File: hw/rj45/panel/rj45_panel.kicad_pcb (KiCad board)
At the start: 6 copper layers, 71.4 x 107 mm, 471 parts, among them J1 SFP edge (INF-8074i), J2 KH-RJ45-58-8P8C, T1 LP72450ANL, U1 RTL8221B-VB-CG, U2 STM32G031F6P6, U3 TPS62822DLC, U4 TPS22918DBVR, X1 MST8011AI-72-33E25

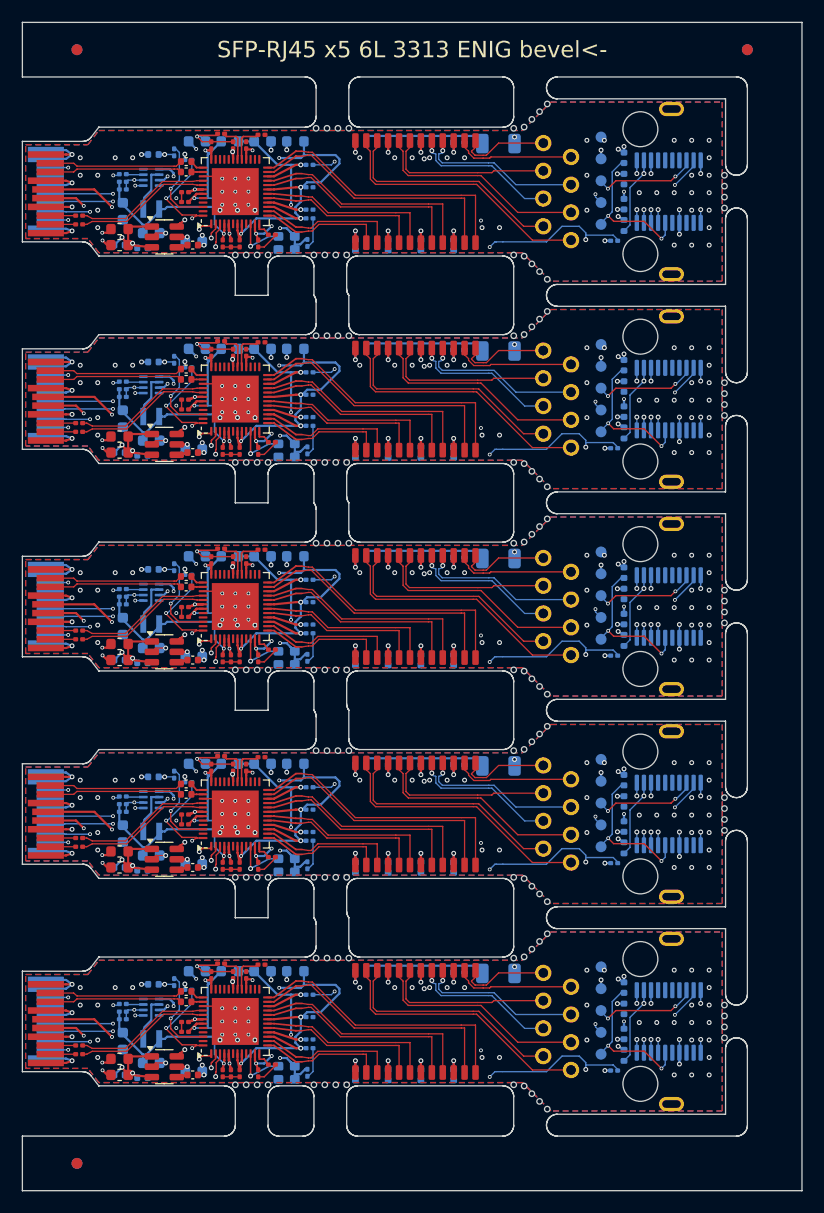
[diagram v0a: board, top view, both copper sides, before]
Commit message: RJ45: PHY address straps on LED0/1/2, re-routed: DRC 0 / 0, KiCad 9 PASS, panel 0 errors
The RTL8221B's CONFIG pins have no internal pulls (datasheet 7.18), so
LED0/1/2 (PHYAD[2:0]) floated. R19-R21, 4.7k to ground: PHYAD 000, which the
PHY maps to address 1 (Table 16 note 2), the firmware's address. Three 0201s
above pins 33-35; C16 moved underneath its via, C17 0.3 mm west.

R11 (INT's pull-up) moved under INT's In2 via. Two links the router left
open are laid by hand before routing (VCCR finger to FB2 through In2, R4's
feedback end through In2); one fresh Freerouting session around them is
kept as rj45.ses.

sfpgen, for board rebuilds:
- plane_dogbones' no-room fallback no longer lays a pad-centre copy of a
  link the pad already has through hand-laid copper (it ran a +3V3 stub
  into the edge strip, and the n <= n0 DRC count let it through);
- drop_duplicate_plane_vias also drops GND router vias inside a locked GND
  via, and the later of two locked same-net vias on top of each other.

KiCad 7 DRC 0 / 0 unconnected, ERC 0; KiCad 9 DRC 0 errors, parity clean,
ERC 0 errors; panel 0 errors, 0 unconnected; edge pins as SFF-8419.
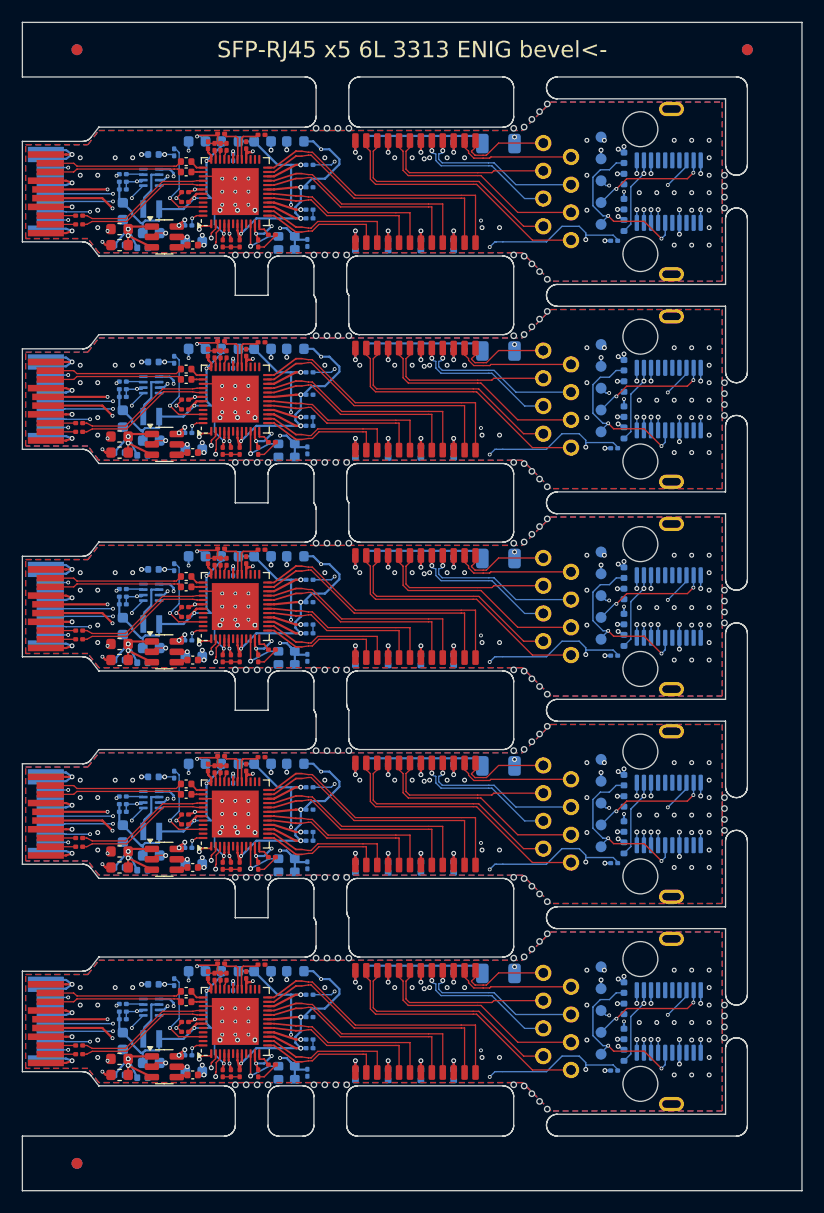
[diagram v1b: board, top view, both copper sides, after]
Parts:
- removed the C16 at (132.1, 88.2)
- removed the C16 at (132.1, 50.2)
- removed the C16 at (132.1, 107.2)
- removed the C16 at (132.1, 69.2)
- removed the C16 at (132.1, 31.2)
- removed the C17 at (130.1, 88.2)
- removed the C17 at (130.1, 69.2)
- removed the C17 at (130.1, 50.2)
- removed the C17 at (130.1, 107.2)
- removed the C17 at (130.1, 31.2)
- removed KiKit_MB_15_5, KiKit_MB_21_5, KiKit_MB_27_5, KiKit_MB_3_5, KiKit_MB_9_5: NPTH, NPTH
- removed the R11 at (128.0, 32.6)
- removed the R11 at (128.0, 51.6)
- removed the R11 at (128.0, 108.6)
- removed the R11 at (128.0, 89.6)
- removed the R11 at (128.0, 70.6)
- added C16: 100nF, Capacitor_SMD:C_0201_0603Metric, B.Cu at (132.1, 32.4)
- added C16: 100nF, Capacitor_SMD:C_0201_0603Metric, B.Cu at (132.1, 108.3)
- added C16: 100nF, Capacitor_SMD:C_0201_0603Metric, B.Cu at (132.1, 51.4)
- added C16: 100nF, Capacitor_SMD:C_0201_0603Metric, B.Cu at (132.1, 89.3)
- added C16: 100nF, Capacitor_SMD:C_0201_0603Metric, B.Cu at (132.1, 70.3)
- added C17: 100nF, Capacitor_SMD:C_0201_0603Metric, F.Cu at (129.8, 50.2)
- added C17: 100nF, Capacitor_SMD:C_0201_0603Metric, F.Cu at (129.8, 69.2)
- added C17: 100nF, Capacitor_SMD:C_0201_0603Metric, F.Cu at (129.8, 31.2)
- added C17: 100nF, Capacitor_SMD:C_0201_0603Metric, F.Cu at (129.8, 107.2)
- added C17: 100nF, Capacitor_SMD:C_0201_0603Metric, F.Cu at (129.8, 88.2)
- added KiKit_MB_12_5: NPTH, NPTH, F.Cu at (160.9, 46.5)
- added KiKit_MB_18_5: NPTH, NPTH, F.Cu at (160.9, 65.5)
- added KiKit_MB_24_5: NPTH, NPTH, F.Cu at (160.9, 84.5)
- added KiKit_MB_30_5: NPTH, NPTH, F.Cu at (160.9, 103.5)
- added KiKit_MB_6_5: NPTH, NPTH, F.Cu at (160.9, 27.5)
- added R11: 4.7k, Resistor_SMD:R_0201_0603Metric, B.Cu at (128.0, 38.6)
- added R11: 4.7k, Resistor_SMD:R_0201_0603Metric, B.Cu at (128.0, 76.6)
- added R11: 4.7k, Resistor_SMD:R_0201_0603Metric, B.Cu at (128.0, 95.6)
- added R11: 4.7k, Resistor_SMD:R_0201_0603Metric, B.Cu at (128.0, 57.6)
- added R11: 4.7k, Resistor_SMD:R_0201_0603Metric, B.Cu at (128.0, 114.6)
- added R19: 4.7k, Resistor_SMD:R_0201_0603Metric, F.Cu at (131.5, 50.4)
- added R19: 4.7k, Resistor_SMD:R_0201_0603Metric, F.Cu at (131.5, 107.4)
- added R19: 4.7k, Resistor_SMD:R_0201_0603Metric, F.Cu at (131.5, 88.4)
- added R19: 4.7k, Resistor_SMD:R_0201_0603Metric, F.Cu at (131.5, 69.4)
- added R19: 4.7k, Resistor_SMD:R_0201_0603Metric, F.Cu at (131.5, 31.4)
- added R20: 4.7k, Resistor_SMD:R_0201_0603Metric, F.Cu at (130.9, 50.4)
- added R20: 4.7k, Resistor_SMD:R_0201_0603Metric, F.Cu at (130.9, 107.4)
- added R20: 4.7k, Resistor_SMD:R_0201_0603Metric, F.Cu at (130.9, 88.4)
- added R20: 4.7k, Resistor_SMD:R_0201_0603Metric, F.Cu at (130.9, 69.4)
- added R20: 4.7k, Resistor_SMD:R_0201_0603Metric, F.Cu at (130.9, 31.4)
- added R21: 4.7k, Resistor_SMD:R_0201_0603Metric, F.Cu at (130.4, 107.4)
- added R21: 4.7k, Resistor_SMD:R_0201_0603Metric, F.Cu at (130.4, 88.4)
- added R21: 4.7k, Resistor_SMD:R_0201_0603Metric, F.Cu at (130.4, 50.4)
- added R21: 4.7k, Resistor_SMD:R_0201_0603Metric, F.Cu at (130.4, 69.4)
- added R21: 4.7k, Resistor_SMD:R_0201_0603Metric, F.Cu at (130.4, 31.4)
- moved KiKit_MB_13_4 37.8 mm to (139.5, 79.3)
- moved KiKit_MB_19_4 37.8 mm to (139.5, 98.3)
- moved KiKit_MB_1_4 37.8 mm to (139.5, 41.3)
- moved KiKit_MB_25_4 37.8 mm to (139.5, 117.3)
- moved KiKit_MB_7_4 37.8 mm to (139.5, 60.3)
- moved KiKit_MB_13_3 37.0 mm to (140.5, 79.3)
- moved KiKit_MB_19_3 37.0 mm to (140.5, 98.3)
- moved KiKit_MB_1_3 37.0 mm to (140.5, 41.3)
- moved KiKit_MB_25_3 37.0 mm to (140.5, 117.3)
- moved KiKit_MB_7_3 37.0 mm to (140.5, 60.3)
- moved KiKit_MB_13_2 36.2 mm to (141.5, 79.3)
- moved KiKit_MB_19_2 36.2 mm to (141.5, 98.3)
- moved KiKit_MB_1_2 36.2 mm to (141.5, 41.3)
- moved KiKit_MB_25_2 36.2 mm to (141.5, 117.3)
- moved KiKit_MB_7_2 36.2 mm to (141.5, 60.3)
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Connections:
- U1 pad 33: Board_3-unconnected-(U1-LED0/PHYAD0-Pad33) -> Board_3-LED0
- U1 pad 34: Board_3-unconnected-(U1-LED1/PHYAD1-Pad34) -> Board_3-LED1
- U1 pad 35: Board_3-unconnected-(U1-LED2/PHYAD2-Pad35) -> Board_3-LED2
- U1 pad 33: Board_4-unconnected-(U1-LED0/PHYAD0-Pad33) -> Board_4-LED0
- U1 pad 34: Board_4-unconnected-(U1-LED1/PHYAD1-Pad34) -> Board_4-LED1
- U1 pad 35: Board_4-unconnected-(U1-LED2/PHYAD2-Pad35) -> Board_4-LED2
- U1 pad 33: Board_0-unconnected-(U1-LED0/PHYAD0-Pad33) -> Board_0-LED0
- U1 pad 34: Board_0-unconnected-(U1-LED1/PHYAD1-Pad34) -> Board_0-LED1
- U1 pad 35: Board_0-unconnected-(U1-LED2/PHYAD2-Pad35) -> Board_0-LED2
- U1 pad 33: Board_2-unconnected-(U1-LED0/PHYAD0-Pad33) -> Board_2-LED0
- U1 pad 34: Board_2-unconnected-(U1-LED1/PHYAD1-Pad34) -> Board_2-LED1
- U1 pad 35: Board_2-unconnected-(U1-LED2/PHYAD2-Pad35) -> Board_2-LED2
- U1 pad 33: Board_1-unconnected-(U1-LED0/PHYAD0-Pad33) -> Board_1-LED0
- U1 pad 34: Board_1-unconnected-(U1-LED1/PHYAD1-Pad34) -> Board_1-LED1
- U1 pad 35: Board_1-unconnected-(U1-LED2/PHYAD2-Pad35) -> Board_1-LED2
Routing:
- net Board_4-PHY_INT_N: track 53.5 -> 46.1 mm, vias 3 -> 2
- net Board_3-PHY_INT_N: track 53.5 -> 46.1 mm, vias 3 -> 2
- net Board_2-PHY_INT_N: track 53.5 -> 46.1 mm, vias 3 -> 2
- net Board_0-PHY_INT_N: track 53.5 -> 46.1 mm, vias 3 -> 2
- net Board_1-PHY_INT_N: track 53.5 -> 46.1 mm, vias 3 -> 2
- net Board_3-+3V3: track 43.7 -> 40.1 mm
- net Board_4-+3V3: track 43.7 -> 40.1 mm
- net Board_2-+3V3: track 43.7 -> 40.1 mm
- net Board_0-+3V3: track 43.7 -> 40.1 mm
- net Board_1-+3V3: track 43.7 -> 40.1 mm
- net Board_3-GND: track 45.3 -> 42.8 mm
- net Board_4-GND: track 45.3 -> 42.8 mm
- net Board_2-GND: track 45.3 -> 42.8 mm
- net Board_1-GND: track 45.3 -> 42.8 mm
- net Board_0-GND: track 45.3 -> 42.8 mm
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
